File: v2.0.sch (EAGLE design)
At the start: 237 parts, among them J1 DC-044-A, J10 16p-2.54, J11 16p-2.54, J12 4p-2.54, J2 MICROSD-9P, J3 2p-2.54, J4 2p-2.54, J5 16p-2.54, J6 16p-2.54, J7 16p-2.54, J9 16p-2.54, Q1 32.768khZ@6Pf, Q10 S8550, Q2 SSM3J328R,LF, Q3 BSS138W-7-F, Q4 BSS138W-7-F, Q5 SSM3J328R,LF, Q6 BSS138W-7-F, Q7 BSS138W-7-F, Q8 CJ2305, Q9 S8550, SW1 MK-12C02 G1.5, SW2 MK-12C02 G1.5, SW3 MK-12C02 G1.5, SW4 MK-12C02 G1.5, U1 MCP23017-E/SO, U10 74HCT139D, U11 BZX84C30, U12 SP483ECN-L, U13 FT232RL-SSOP28, U14 FT232RL-SSOP28, U15 FT232RL-SSOP28, U2 MCP79412-I/SN, U3 LOPY, U4 MAX213IDBR, U5 FT232RL-SSOP28, U8 BR24G32-3, Y2 12MHZ

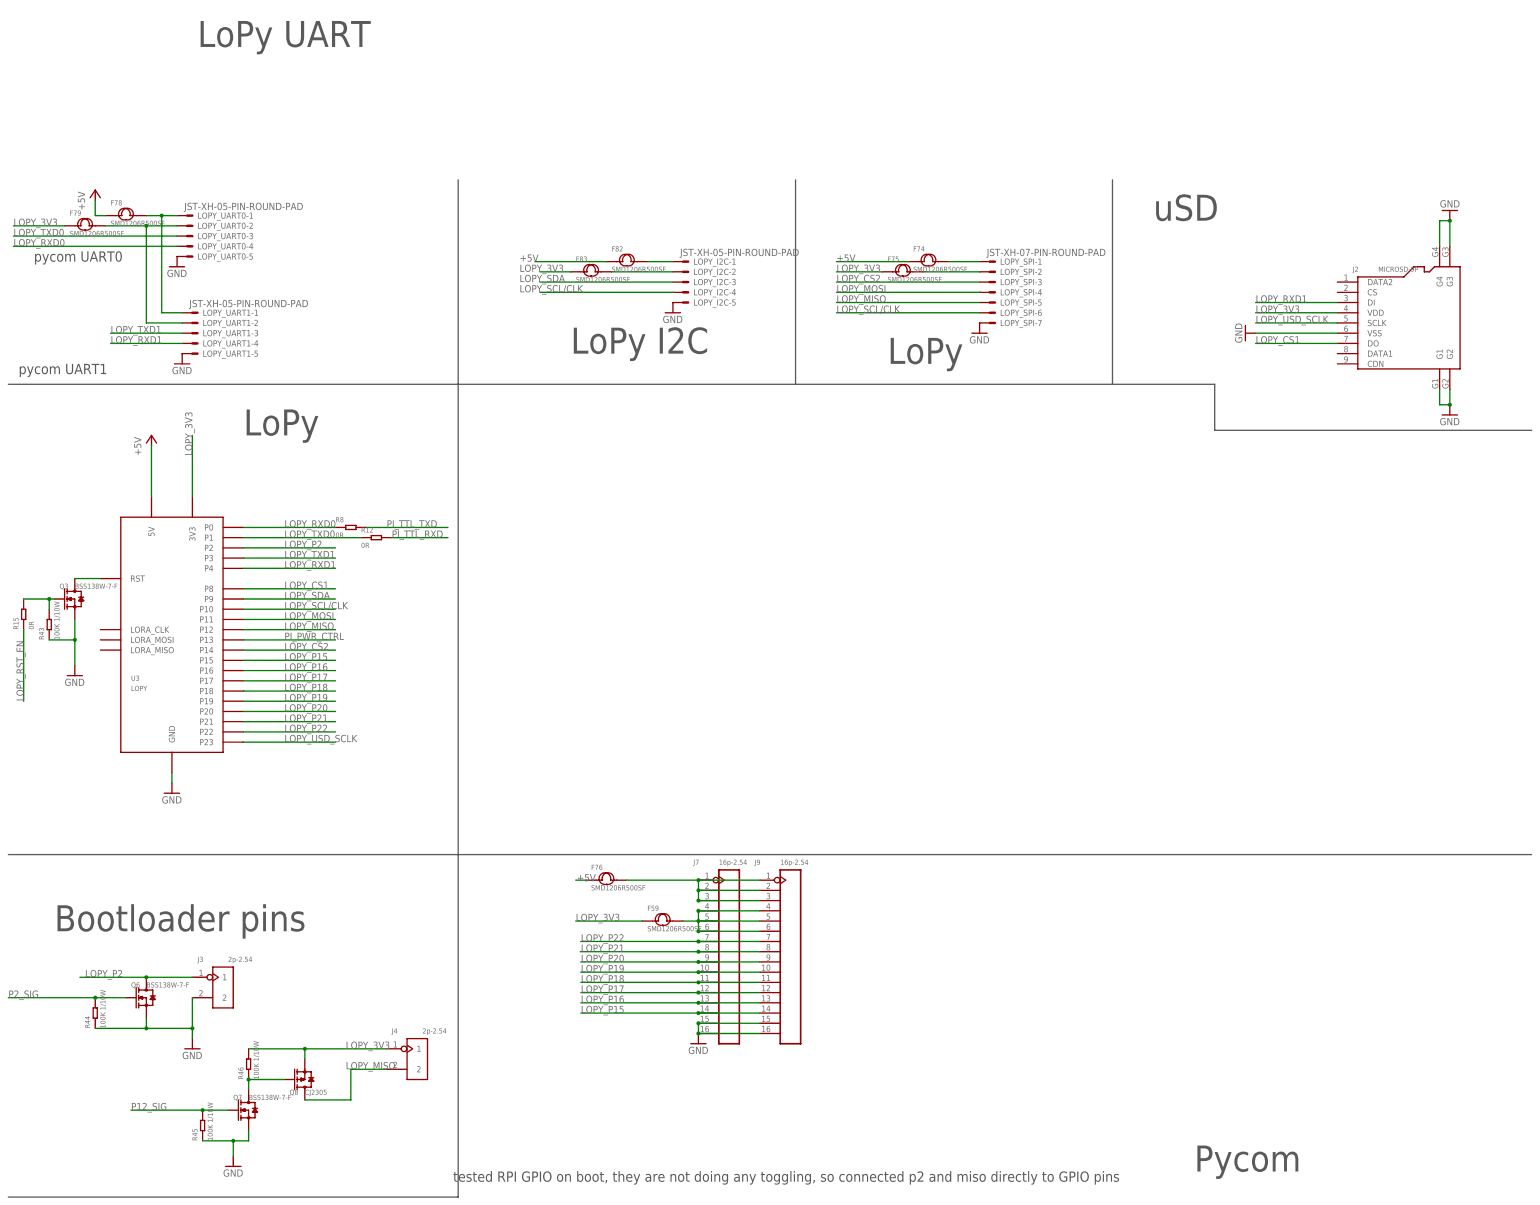
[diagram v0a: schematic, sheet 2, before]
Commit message: V2 laid out
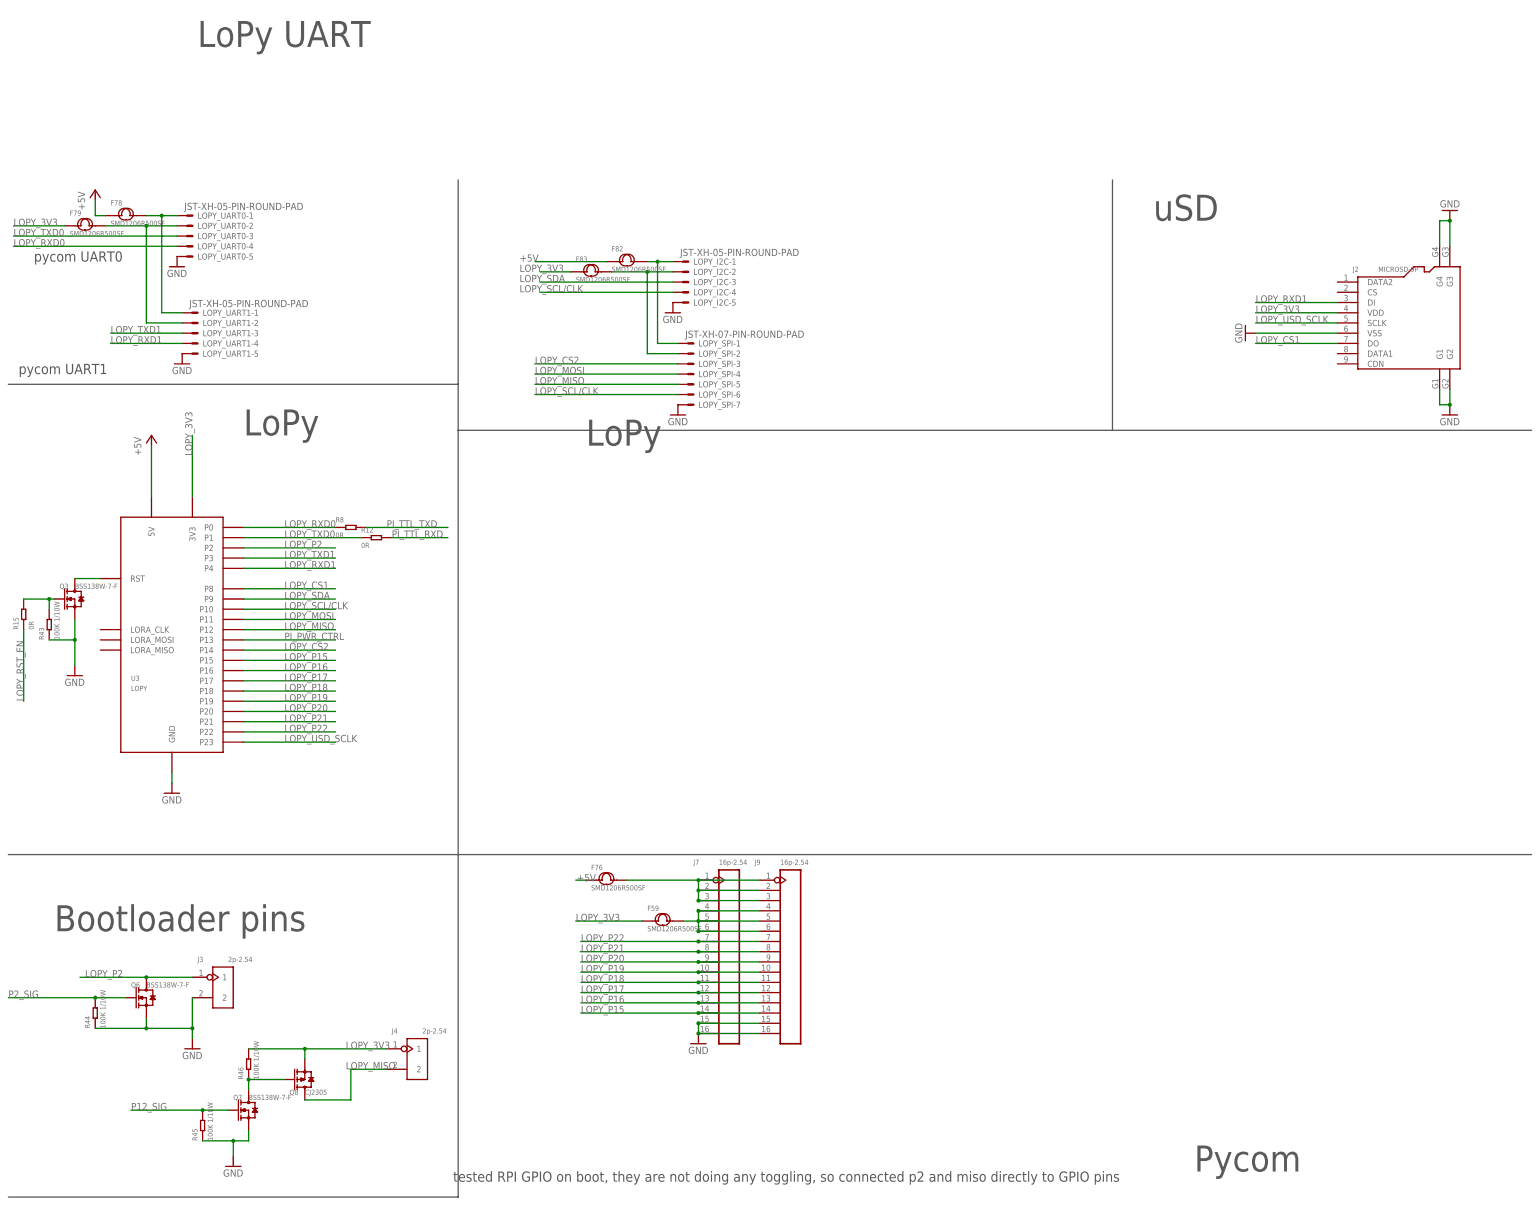
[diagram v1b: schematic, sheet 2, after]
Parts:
- removed F74, F75: SMD1206R500SF, Seeed-Fuse:SMD-PPTC-500MA(1206)
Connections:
- net N$16 renamed P2_EN
- net N$18 renamed PI12_EN
- removed net LOPY_SPI_3V3_PROTECTED: F75.2, LOPY_SPI-2.S
- removed net LOPY_SPI_5V_PROTECTED: F74.2, LOPY_SPI-1.S
- net +5V: no longer F74.1
- net LOPY_3V3: no longer F75.1
- net LOPY_I2C_3V3_PROTECTED: now also LOPY_SPI-2.S
- net N$4: now also LOPY_SPI-1.S
- net N$9: now also SW1.A; no longer SW1.B
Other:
- note removed: "LoPy I2C"
- moved on the sheet: LOPY_SPI-1, LOPY_SPI-2, LOPY_SPI-3, LOPY_SPI-4, LOPY_SPI-5, LOPY_SPI-6, LOPY_SPI-7
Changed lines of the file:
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@@
 <part name="F82" library="Seeed-Fuse" library_urn="urn:adsk.eagle:library:469" deviceset="SMD-PPTC-500MA(1206)" device="" value="SMD1206R500SF"/>
 <part name="F83" library="Seeed-Fuse" library_urn="urn:adsk.eagle:library:469" deviceset="SMD-PPTC-500MA(1206)" device="" value="SMD1206R500SF"/>
-<part name="F74" library="Seeed-Fuse" library_urn="urn:adsk.eagle:library:469" deviceset="SMD-PPTC-500MA(1206)" device="" value="SMD1206R500SF"/>
-<part name="F75" library="Seeed-Fuse" library_urn="urn:adsk.eagle:library:469" deviceset="SMD-PPTC-500MA(1206)" device="" value="SMD1206R500SF"/>
 <part name="F76" library="Seeed-Fuse" library_urn="urn:adsk.eagle:library:469" deviceset="SMD-PPTC-500MA(1206)" device="" value="SMD1206R500SF"/>
 <part name="PI_ADC_1" library="Rembrandt Electronics - JST XH Connectors v1-0 2" deviceset="JST-XH-07-PIN" device="-ROUND-PAD"/>
@@
 </segment>
 </net>
-<net name="N$16" class="0">
+<net name="P2_EN" class="0">
 <segment>
 <pinref part="R41" gate="G$1" pin="1"/>
@@
 </segment>
 </net>
-<net name="N$18" class="0">
+<net name="PI12_EN" class="0">
 <segment>
 <pinref part="U1" gate="A" pin="GPB6"/>
@@
 <text x="-5.08" y="175.26" size="2.54" layer="97">pycom UART1</text>
 <text x="-1.27" y="203.2" size="2.54" layer="97">pycom UART0</text>
-<wire x1="104.14" y1="172.72" x2="187.96" y2="172.72" width="0.1524" layer="97"/>
-<wire x1="187.96" y1="172.72" x2="187.96" y2="223.52" width="0.1524" layer="97"/>
-<wire x1="187.96" y1="172.72" x2="266.7" y2="172.72" width="0.1524" layer="97"/>
-<wire x1="266.7" y1="172.72" x2="266.7" y2="223.52" width="0.1524" layer="97"/>
-<text x="132.08" y="180.34" size="6.4516" layer="97">LoPy I2C</text>
-<text x="210.82" y="177.8" size="6.4516" layer="97">LoPy</text>
+<wire x1="104.14" y1="161.29" x2="266.7" y2="161.29" width="0.1524" layer="97"/>
+<wire x1="266.7" y1="161.29" x2="266.7" y2="223.52" width="0.1524" layer="97"/>
+<text x="135.89" y="157.48" size="6.4516" layer="97">LoPy</text>
 <text x="39.37" y="256.54" size="6.4516" layer="97">LoPy UART</text>
 <wire x1="-7.62" y1="55.88" x2="104.14" y2="55.88" width="0.1524" layer="97"/>
-<wire x1="104.14" y1="55.88" x2="104.14" y2="172.72" width="0.1524" layer="97"/>
-<wire x1="370.84" y1="161.29" x2="292.1" y2="161.29" width="0.1524" layer="97"/>
-<wire x1="292.1" y1="161.29" x2="292.1" y2="172.72" width="0.1524" layer="97"/>
-<wire x1="292.1" y1="172.72" x2="266.7" y2="172.72" width="0.1524" layer="97"/>
+<wire x1="104.14" y1="55.88" x2="104.14" y2="161.29" width="0.1524" layer="97"/>
+<wire x1="104.14" y1="161.29" x2="104.14" y2="172.72" width="0.1524" layer="97"/>
+<wire x1="370.84" y1="161.29" x2="266.7" y2="161.29" width="0.1524" layer="97"/>
 <wire x1="104.14" y1="55.88" x2="370.84" y2="55.88" width="0.1524" layer="97"/>
 <text x="50.8" y="160.02" size="6.4516" layer="97">LoPy</text>
@@
 <instance part="LOPY_I2C" gate="-5" x="160.02" y="193.04"/>
 <instance part="J2" gate="G$1" x="340.36" y="187.96"/>
-<instance part="LOPY_SPI" gate="-1" x="236.22" y="203.2"/>
-<instance part="LOPY_SPI" gate="-2" x="236.22" y="200.66"/>
-<instance part="LOPY_SPI" gate="-3" x="236.22" y="198.12"/>
-<instance part="LOPY_SPI" gate="-4" x="236.22" y="195.58"/>
-<instance part="LOPY_SPI" gate="-5" x="236.22" y="193.04"/>
-<instance part="LOPY_SPI" gate="-6" x="236.22" y="190.5"/>
-<instance part="LOPY_SPI" gate="-7" x="236.22" y="187.96"/>
+<instance part="LOPY_SPI" gate="-1" x="161.29" y="182.88"/>
+<instance part="LOPY_SPI" gate="-2" x="161.29" y="180.34"/>
+<instance part="LOPY_SPI" gate="-3" x="161.29" y="177.8"/>
+<instance part="LOPY_SPI" gate="-4" x="161.29" y="175.26"/>
+<instance part="LOPY_SPI" gate="-5" x="161.29" y="172.72"/>
+<instance part="LOPY_SPI" gate="-6" x="161.29" y="170.18"/>
+<instance part="LOPY_SPI" gate="-7" x="161.29" y="167.64"/>
 <instance part="GND35" gate="1" x="350.52" y="165.1"/>
 <instance part="GND36" gate="1" x="350.52" y="215.9" rot="R180"/>
@@
 <instance part="F82" gate="G$1" x="146.05" y="203.2"/>
 <instance part="F83" gate="G$1" x="137.16" y="200.66"/>
-<instance part="F74" gate="G$1" x="220.98" y="203.2"/>
-<instance part="F75" gate="G$1" x="214.63" y="200.66"/>
 <instance part="F76" gate="G$1" x="140.97" y="49.53"/>
 <instance part="F59" gate="G$1" x="154.94" y="39.37"/>
 <instance part="GND38" gate="1" x="163.83" y="8.89"/>
 <instance part="GND42" gate="1" x="299.72" y="185.42" rot="R270"/>
-<instance part="GND43" gate="1" x="233.68" y="185.42"/>
+<instance part="GND43" gate="1" x="158.75" y="165.1"/>
 <instance part="GND52" gate="1" x="157.48" y="190.5"/>
 <instance part="GND54" gate="1" x="35.56" y="177.8"/>
@@
 </segment>
 <segment>
-<label x="198.12" y="203.2" size="1.778" layer="95"/>
-<pinref part="F74" gate="G$1" pin="1"/>
-<wire x1="215.9" y1="203.2" x2="198.12" y2="203.2" width="0.1524" layer="91"/>
-</segment>
-<segment>
 <pinref part="F76" gate="G$1" pin="1"/>
 <wire x1="135.89" y1="49.53" x2="133.35" y2="49.53" width="0.1524" layer="91"/>
@@
 </segment>
 <segment>
-<pinref part="F75" gate="G$1" pin="1"/>
-<wire x1="209.55" y1="200.66" x2="198.12" y2="200.66" width="0.1524" layer="91"/>
-<label x="198.12" y="200.66" size="1.778" layer="95"/>
-</segment>
-<segment>
 <pinref part="F79" gate="G$1" pin="1"/>
 <wire x1="6.35" y1="212.09" x2="-6.35" y2="212.09" width="0.1524" layer="91"/>
@@
 <segment>
 <pinref part="LOPY_SPI" gate="-6" pin="S"/>
-<wire x1="233.68" y1="190.5" x2="198.12" y2="190.5" width="0.1524" layer="91"/>
-<label x="198.12" y="190.5" size="1.778" layer="95"/>
+<wire x1="158.75" y1="170.18" x2="123.19" y2="170.18" width="0.1524" layer="91"/>
+<label x="123.19" y="170.18" size="1.778" layer="95"/>
 </segment>
 <segment>
@@
 <segment>
 <pinref part="LOPY_SPI" gate="-4" pin="S"/>
-<wire x1="233.68" y1="195.58" x2="198.12" y2="195.58" width="0.1524" layer="91"/>
-<label x="198.12" y="195.58" size="1.778" layer="95"/>
+<wire x1="158.75" y1="175.26" x2="123.19" y2="175.26" width="0.1524" layer="91"/>
+<label x="123.19" y="175.26" size="1.778" layer="95"/>
 </segment>
 </net>
@@
 <segment>
 <pinref part="LOPY_SPI" gate="-5" pin="S"/>
-<wire x1="233.68" y1="193.04" x2="198.12" y2="193.04" width="0.1524" layer="91"/>
-<label x="198.12" y="193.04" size="1.778" layer="95"/>
+<wire x1="158.75" y1="172.72" x2="123.19" y2="172.72" width="0.1524" layer="91"/>
+<label x="123.19" y="172.72" size="1.778" layer="95"/>
 </segment>
 <segment>
@@
 <segment>
 <pinref part="LOPY_SPI" gate="-3" pin="S"/>
-<wire x1="233.68" y1="198.12" x2="198.12" y2="198.12" width="0.1524" layer="91"/>
-<label x="198.12" y="198.12" size="1.778" layer="95"/>
+<wire x1="158.75" y1="177.8" x2="123.19" y2="177.8" width="0.1524" layer="91"/>
+<label x="123.19" y="177.8" size="1.778" layer="95"/>
 </segment>
 </net>
@@
 <pinref part="F83" gate="G$1" pin="2"/>
 <pinref part="LOPY_I2C" gate="-2" pin="S"/>
-<wire x1="142.24" y1="200.66" x2="157.48" y2="200.66" width="0.1524" layer="91"/>
-</segment>
-</net>
-<net name="LOPY_SPI_5V_PROTECTED" class="0">
-<segment>
-<pinref part="LOPY_SPI" gate="-1" pin="S"/>
-<wire x1="233.68" y1="203.2" x2="226.06" y2="203.2" width="0.1524" layer="91"/>
-<pinref part="F74" gate="G$1" pin="2"/>
-</segment>
-</net>
-<net name="LOPY_SPI_3V3_PROTECTED" class="0">
-<segment>
-<pinref part="F75" gate="G$1" pin="2"/>
+<wire x1="142.24" y1="200.66" x2="151.13" y2="200.66" width="0.1524" layer="91"/>
 <pinref part="LOPY_SPI" gate="-2" pin="S"/>
-<wire x1="219.71" y1="200.66" x2="233.68" y2="200.66" width="0.1524" layer="91"/>
+<wire x1="151.13" y1="200.66" x2="157.48" y2="200.66" width="0.1524" layer="91"/>
+<wire x1="158.75" y1="180.34" x2="151.13" y2="180.34" width="0.1524" layer="91"/>
+<wire x1="151.13" y1="180.34" x2="151.13" y2="200.66" width="0.1524" layer="91"/>
+<junction x="151.13" y="200.66"/>
 </segment>
 </net>
@@
 <pinref part="LOPY_I2C" gate="-1" pin="S"/>
 <pinref part="F82" gate="G$1" pin="2"/>
-<wire x1="157.48" y1="203.2" x2="151.13" y2="203.2" width="0.1524" layer="91"/>
+<wire x1="157.48" y1="203.2" x2="153.67" y2="203.2" width="0.1524" layer="91"/>
+<pinref part="LOPY_SPI" gate="-1" pin="S"/>
+<wire x1="153.67" y1="203.2" x2="151.13" y2="203.2" width="0.1524" layer="91"/>
+<wire x1="158.75" y1="182.88" x2="153.67" y2="182.88" width="0.1524" layer="91"/>
+<wire x1="153.67" y1="182.88" x2="153.67" y2="203.2" width="0.1524" layer="91"/>
+<junction x="153.67" y="203.2"/>
 </segment>
 </net>
@@
 <wire x1="314.96" y1="187.96" x2="313.69" y2="187.96" width="0.1524" layer="91"/>
 <pinref part="R25" gate="G$1" pin="1"/>
-<pinref part="SW1" gate="G$1" pin="B"/>
-<wire x1="299.72" y1="193.04" x2="299.72" y2="190.5" width="0.1524" layer="91"/>
-<wire x1="299.72" y1="190.5" x2="313.69" y2="190.5" width="0.1524" layer="91"/>
 <wire x1="313.69" y1="190.5" x2="313.69" y2="187.96" width="0.1524" layer="91"/>
 <junction x="313.69" y="187.96"/>
+<pinref part="SW1" gate="G$1" pin="A"/>
+<wire x1="313.69" y1="190.5" x2="309.88" y2="190.5" width="0.1524" layer="91"/>
+<wire x1="309.88" y1="190.5" x2="309.88" y2="193.04" width="0.1524" layer="91"/>
 </segment>
 </net>
